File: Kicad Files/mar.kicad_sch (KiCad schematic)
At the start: 37 parts, among them U10 74LS173, U11 74LS173, U12 74LS173, U9 74LS173

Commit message: im sooo stupiiid
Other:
- moved on the sheet: C10, D45, D46, D47, D48, D49, D50, D51, D52, D53, D54, D55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

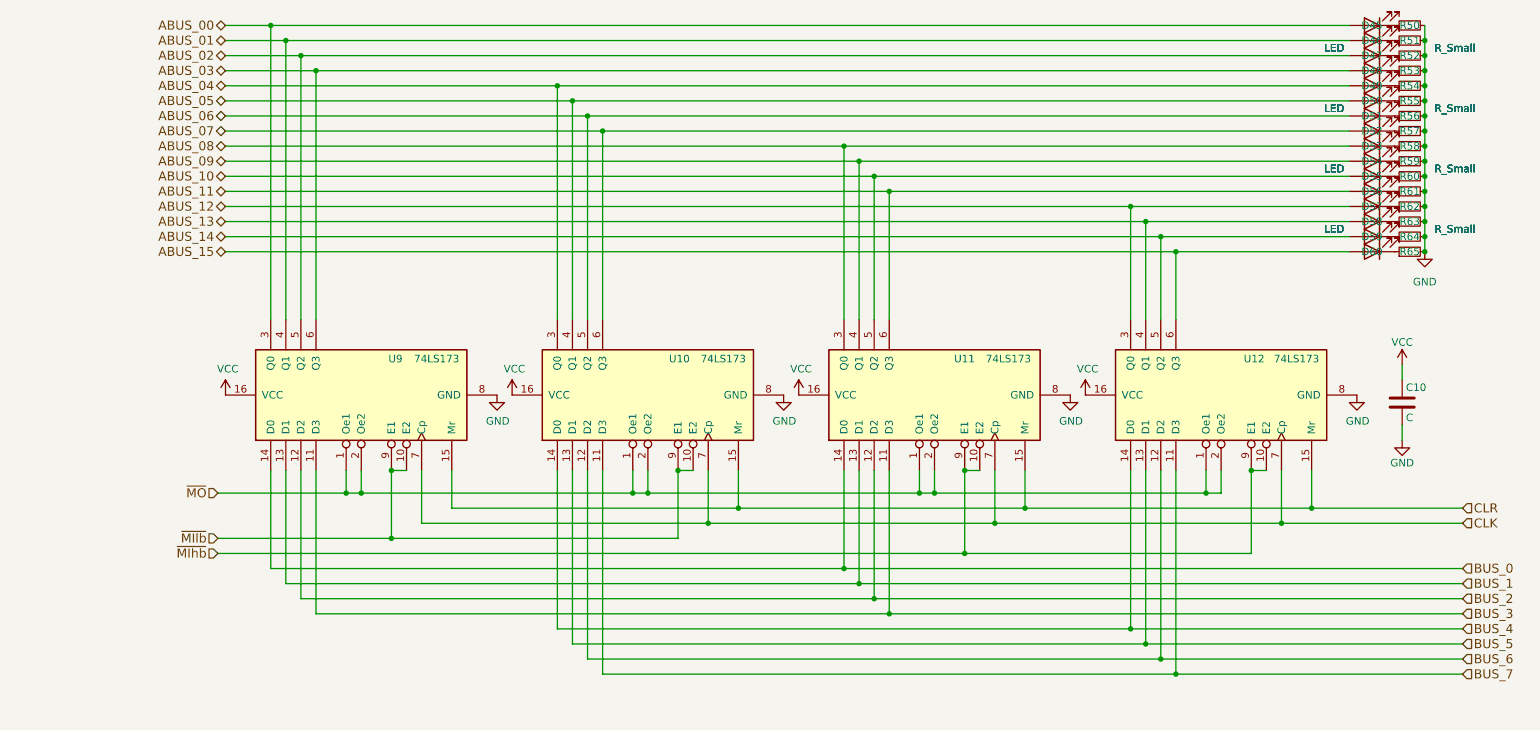
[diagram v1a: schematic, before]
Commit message: complete redraw to bus system
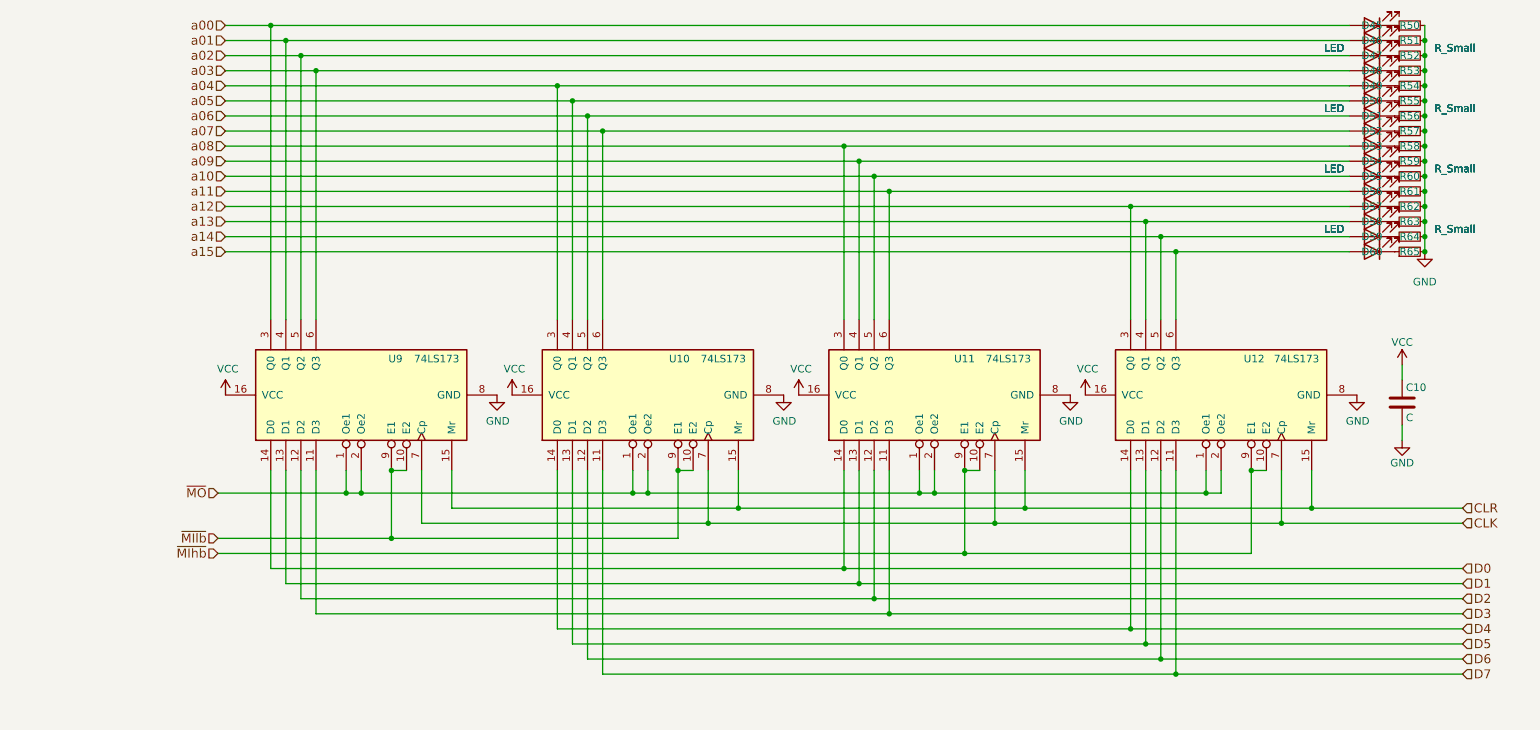
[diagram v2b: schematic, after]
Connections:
- net ABUS_00 renamed a00
- net ABUS_01 renamed a01
- net ABUS_02 renamed a02
- net ABUS_03 renamed a03
- net ABUS_04 renamed a04
- net ABUS_05 renamed a05
- net ABUS_06 renamed a06
- net ABUS_07 renamed a07
- net ABUS_08 renamed a08
- net ABUS_09 renamed a09
- net ABUS_10 renamed a10
- net ABUS_11 renamed a11
- net ABUS_12 renamed a12
- net ABUS_13 renamed a13
- net ABUS_14 renamed a14
- net ABUS_15 renamed a15
- net BUS_0 renamed D0
- net BUS_1 renamed D1
- net BUS_2 renamed D2
- net BUS_3 renamed D3
- net BUS_4 renamed D4
- net BUS_5 renamed D5
- net BUS_6 renamed D6
- net BUS_7 renamed D7
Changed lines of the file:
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@@
     (stroke (width 0) (type default) (color 0 0 0 0))
   )
-  (hierarchical_label "BUS_4" (shape input) (at 255.27 135.89 0)
+  (hierarchical_label "a07" (shape input) (at 46.99 52.07 180)
+    (effects (font (size 1.524 1.524)) (justify right))
+  )
+  (hierarchical_label "D4" (shape input) (at 255.27 135.89 0)
     (effects (font (size 1.524 1.524)) (justify left))
   )
-  (hierarchical_label "ABUS_08" (shape tri_state) (at 46.99 54.61 180)
-    (effects (font (size 1.524 1.524)) (justify right))
-  )
-  (hierarchical_label "ABUS_05" (shape tri_state) (at 46.99 46.99 180)
-    (effects (font (size 1.524 1.524)) (justify right))
-  )
-  (hierarchical_label "ABUS_02" (shape tri_state) (at 46.99 39.37 180)
-    (effects (font (size 1.524 1.524)) (justify right))
-  )
   (hierarchical_label "~{MIlb}" (shape input) (at 45.72 120.65 180)
-    (effects (font (size 1.524 1.524)) (justify right))
-  )
-  (hierarchical_label "ABUS_11" (shape tri_state) (at 46.99 62.23 180)
     (effects (font (size 1.524 1.524)) (justify right))
   )
@@
     (effects (font (size 1.524 1.524)) (justify right))
   )
-  (hierarchical_label "ABUS_07" (shape tri_state) (at 46.99 52.07 180)
+  (hierarchical_label "a09" (shape input) (at 46.99 57.15 180)
     (effects (font (size 1.524 1.524)) (justify right))
   )
-  (hierarchical_label "ABUS_14" (shape tri_state) (at 46.99 69.85 180)
+  (hierarchical_label "a13" (shape input) (at 46.99 67.31 180)
+    (effects (font (size 1.524 1.524)) (justify right))
+  )
+  (hierarchical_label "a11" (shape input) (at 46.99 62.23 180)
+    (effects (font (size 1.524 1.524)) (justify right))
+  )
+  (hierarchical_label "a03" (shape input) (at 46.99 41.91 180)
     (effects (font (size 1.524 1.524)) (justify right))
   )
@@
     (effects (font (size 1.524 1.524)) (justify left))
   )
-  (hierarchical_label "ABUS_06" (shape tri_state) (at 46.99 49.53 180)
+  (hierarchical_label "a04" (shape input) (at 46.99 44.45 180)
     (effects (font (size 1.524 1.524)) (justify right))
   )
-  (hierarchical_label "BUS_6" (shape input) (at 255.27 140.97 0)
+  (hierarchical_label "D6" (shape input) (at 255.27 140.97 0)
     (effects (font (size 1.524 1.524)) (justify left))
   )
-  (hierarchical_label "ABUS_09" (shape tri_state) (at 46.99 57.15 180)
+  (hierarchical_label "a00" (shape input) (at 46.99 34.29 180)
     (effects (font (size 1.524 1.524)) (justify right))
   )
-  (hierarchical_label "BUS_5" (shape input) (at 255.27 138.43 0)
+  (hierarchical_label "D5" (shape input) (at 255.27 138.43 0)
     (effects (font (size 1.524 1.524)) (justify left))
   )
-  (hierarchical_label "BUS_7" (shape input) (at 255.27 143.51 0)
+  (hierarchical_label "D7" (shape input) (at 255.27 143.51 0)
     (effects (font (size 1.524 1.524)) (justify left))
   )
-  (hierarchical_label "BUS_0" (shape input) (at 255.27 125.73 0)
+  (hierarchical_label "D0" (shape input) (at 255.27 125.73 0)
     (effects (font (size 1.524 1.524)) (justify left))
   )
-  (hierarchical_label "BUS_2" (shape input) (at 255.27 130.81 0)
+  (hierarchical_label "D2" (shape input) (at 255.27 130.81 0)
     (effects (font (size 1.524 1.524)) (justify left))
+  )
+  (hierarchical_label "a14" (shape input) (at 46.99 69.85 180)
+    (effects (font (size 1.524 1.524)) (justify right))
+  )
+  (hierarchical_label "a02" (shape input) (at 46.99 39.37 180)
+    (effects (font (size 1.524 1.524)) (justify right))
+  )
+  (hierarchical_label "a05" (shape input) (at 46.99 46.99 180)
+    (effects (font (size 1.524 1.524)) (justify right))
   )
   (hierarchical_label "CLR" (shape input) (at 255.27 115.57 0)
     (effects (font (size 1.524 1.524)) (justify left))
   )
-  (hierarchical_label "ABUS_04" (shape tri_state) (at 46.99 44.45 180)
+  (hierarchical_label "a12" (shape input) (at 46.99 64.77 180)
     (effects (font (size 1.524 1.524)) (justify right))
   )
-  (hierarchical_label "BUS_3" (shape input) (at 255.27 133.35 0)
+  (hierarchical_label "a10" (shape input) (at 46.99 59.69 180)
+    (effects (font (size 1.524 1.524)) (justify right))
+  )
+  (hierarchical_label "D3" (shape input) (at 255.27 133.35 0)
     (effects (font (size 1.524 1.524)) (justify left))
   )
-  (hierarchical_label "BUS_1" (shape input) (at 255.27 128.27 0)
+  (hierarchical_label "D1" (shape input) (at 255.27 128.27 0)
     (effects (font (size 1.524 1.524)) (justify left))
   )
-  (hierarchical_label "ABUS_03" (shape tri_state) (at 46.99 41.91 180)
+  (hierarchical_label "a06" (shape input) (at 46.99 49.53 180)
     (effects (font (size 1.524 1.524)) (justify right))
   )
-  (hierarchical_label "ABUS_00" (shape tri_state) (at 46.99 34.29 180)
+  (hierarchical_label "a15" (shape input) (at 46.99 72.39 180)
     (effects (font (size 1.524 1.524)) (justify right))
   )
@@
     (effects (font (size 1.524 1.524)) (justify right))
   )
-  (hierarchical_label "ABUS_12" (shape tri_state) (at 46.99 64.77 180)
+  (hierarchical_label "a08" (shape input) (at 46.99 54.61 180)
     (effects (font (size 1.524 1.524)) (justify right))
   )
-  (hierarchical_label "ABUS_15" (shape tri_state) (at 46.99 72.39 180)
+  (hierarchical_label "a01" (shape input) (at 46.99 36.83 180)
     (effects (font (size 1.524 1.524)) (justify right))
   )
-  (hierarchical_label "ABUS_10" (shape tri_state) (at 46.99 59.69 180)
-    (effects (font (size 1.524 1.524)) (justify right))
-  )
-  (hierarchical_label "ABUS_13" (shape tri_state) (at 46.99 67.31 180)
-    (effects (font (size 1.524 1.524)) (justify right))
-  )
-  (hierarchical_label "ABUS_01" (shape tri_state) (at 46.99 36.83 180)
-    (effects (font (size 1.524 1.524)) (justify right))
-  )

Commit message: update
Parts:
- removed C10: C, Capacitor_THT:C_Disc_D4.3mm_W1.9mm_P5.00mm, symbol Device:C
- removed D45, D46, D47, D48, D49, D50, D51, D52, D53, D54, D55, D56, D57, D58, D59, D60: LED, symbol Device:LED
- removed R50, R51, R52, R53, R54, R55, R56, R57, R58, R59, R60, R61, R62, R63, R64, R65: R_Small, symbol Device:R_Small
- added D137, D9: LED_Small, symbol Device:LED_Small
- added R146, R9: R_Small, symbol Device:R_Small
- added U27: 74HC00, symbol 74xx:74HC00
- renumbered U9 to U28, U10 to U29, U11 to U30, U12 to U31
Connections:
- net VCC: now also R146.2, R9.2
- net D0 renamed d_{i}0
- net D1 renamed d_{i}1
- net D2 renamed d_{i}2
- net D3 renamed d_{i}3
- net D4 renamed d_{i}4
- net D5 renamed d_{i}5
- net D6 renamed d_{i}6
- net D7 renamed d_{i}7
- net ~{MIhb}: no longer names the net of U30.9 (E1), U31.9 (E1)
- net ~{MIhb}: now also U27.3; no longer U30.10 (E2), U31.10 (E2)
- net ~{MIlb} renamed H/~{L}
- net H/~{L}: now also U27.1, U27.2; no longer U28.10 (E2), U29.10 (E2)
- net ~{MO} renamed ~{M_{O}}
- net ~{M_{O}}: now also D9.1 (K)
- new net: D9.2 (A), R9.1
- new net: D137.2 (A), R146.1
- new net ~{M_{I}}: D137.1 (K), U28.10 (E2), U29.10 (E2), U30.10 (E2), U31.10 (E2)
